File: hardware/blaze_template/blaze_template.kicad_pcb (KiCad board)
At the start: 4 copper layers, 70 x 70 mm, 11 parts, among them J1 FrontInterconnect, J2 RearInterconnect, U1 TCAN1044VDDFR

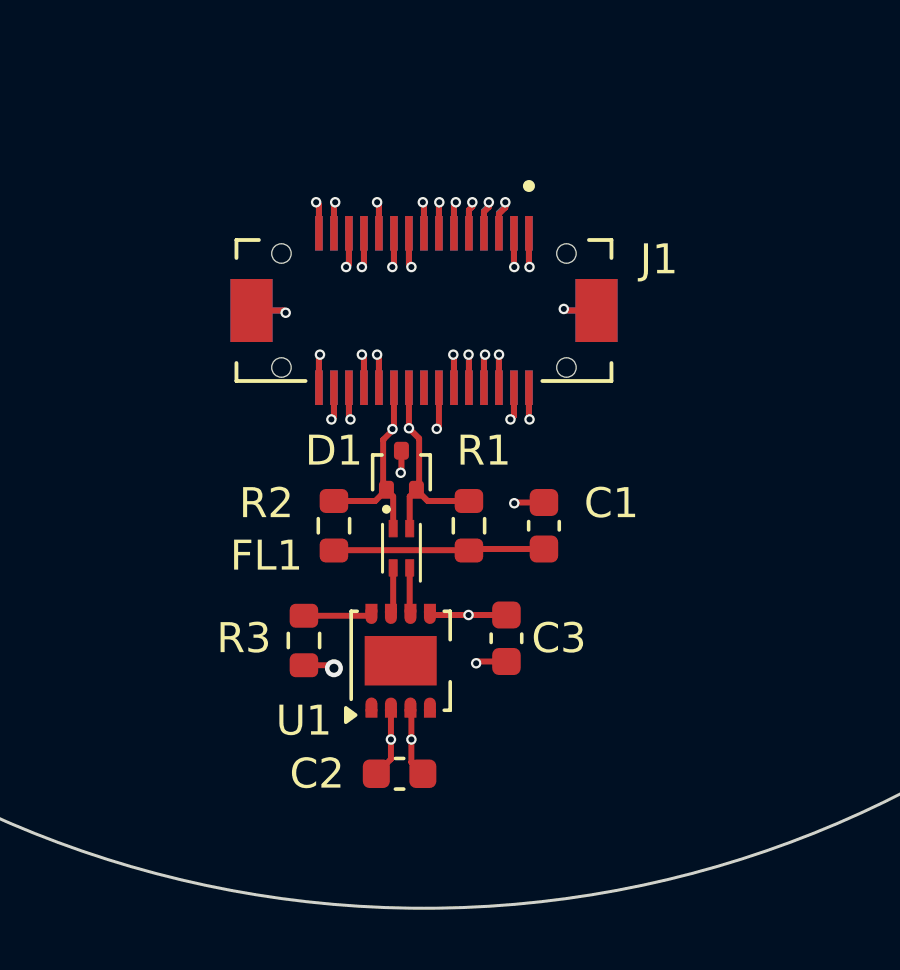
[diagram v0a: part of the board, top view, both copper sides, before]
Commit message: Fixed via size
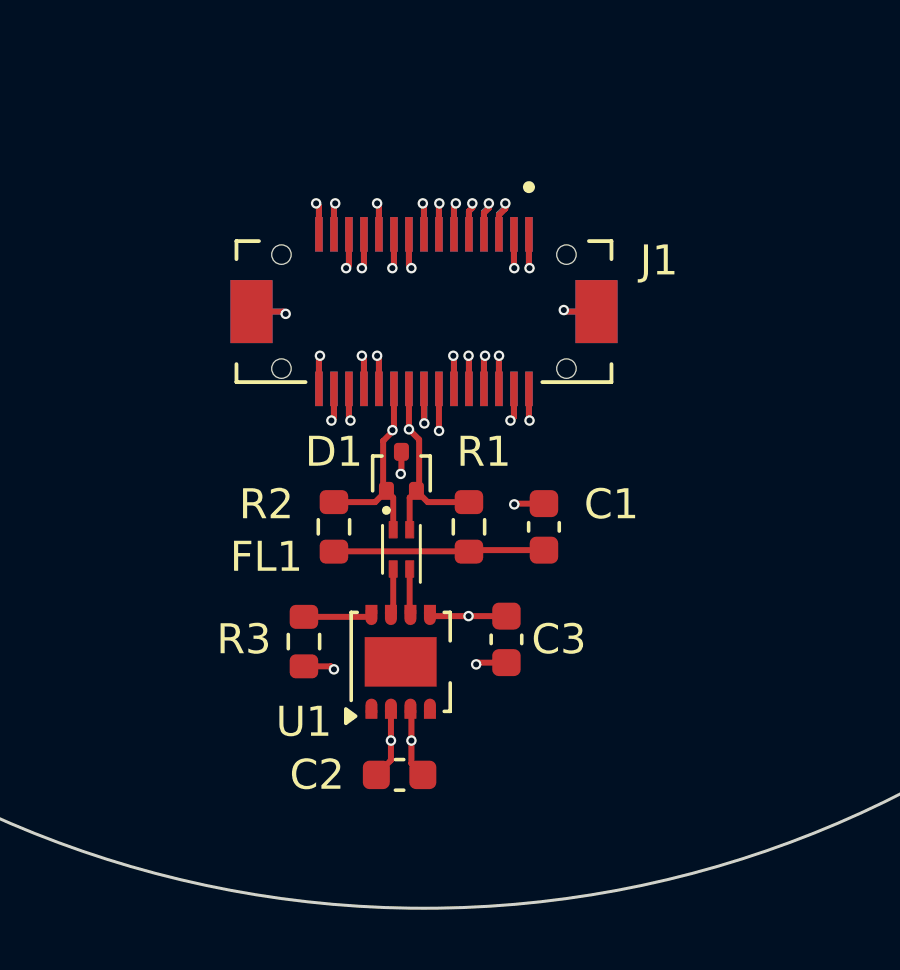
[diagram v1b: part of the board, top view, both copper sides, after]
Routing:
- net Net-(J1-Pin_23): track 0.00 -> 2.31 mm, vias 0 -> 1

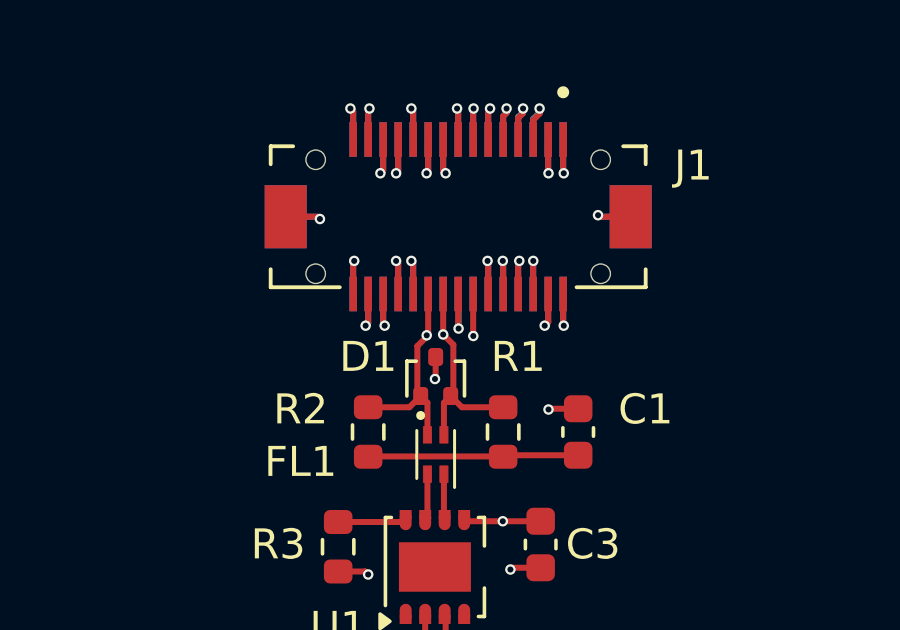
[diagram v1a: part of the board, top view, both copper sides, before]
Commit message: Repaired misisng via connections
CANH, CANL, unassigned, were  not connected on back side
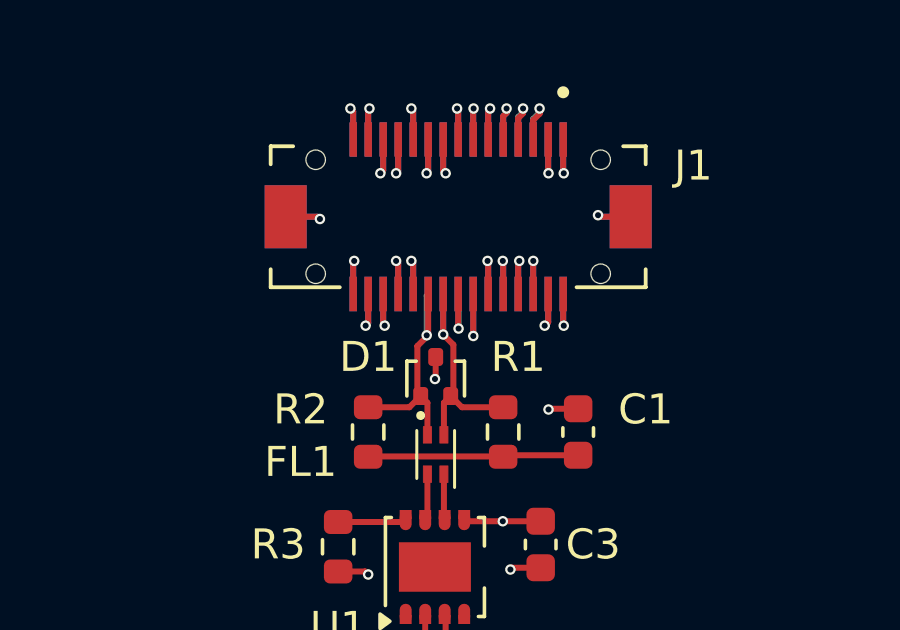
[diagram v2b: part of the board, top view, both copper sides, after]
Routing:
- net Net-(J1-Pin_24): track 1.40 -> 2.80 mm
- net /CANH: track 6.94 -> 8.34 mm
- net /CANL: track 6.90 -> 8.25 mm
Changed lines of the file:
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@@
+	)
+	(segment
+		(start 148 124.537)
+		(end 148 123.187)
+		(width 0.2)
+		(layer "B.Cu")
+		(net 4)
 	)
 	(segment
@@
 	)
 	(segment
+		(start 147.450684 123.236316)
+		(end 147.5 123.187)
+		(width 0.2)
+		(layer "B.Cu")
+		(net 5)
+	)
+	(segment
+		(start 147.450684 124.564466)
+		(end 147.450684 123.236316)
+		(width 0.2)
+		(layer "B.Cu")
+		(net 5)
+	)
+	(segment
 		(start 149.5 117.067006)
 		(end 149.5 118.037)
@@
 		(net 22)
 	)
+	(segment
+		(start 149.004 123.191)
+		(end 149 123.187)
+		(width 0.2)
+		(layer "B.Cu")
+		(net 22)
+	)
+	(segment
+		(start 149.004 124.587)
+		(end 149.004 123.191)
+		(width 0.2)
+		(layer "B.Cu")
+		(net 22)
+	)
